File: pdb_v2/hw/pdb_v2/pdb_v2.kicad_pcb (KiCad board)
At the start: 4 copper layers, 96 x 56 mm, 75 parts, among them J1 XT30-M_Ver, J2 JST-PH_01x02, J3 Conn_01x06_Pin, J4 JST-PH_01x02, J5 JST-PH_01x02, J6 Conn_01x03, J7 Conn_01x03, J8 Conn_01x04, Q1 60Vds, SW1 SW_Push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

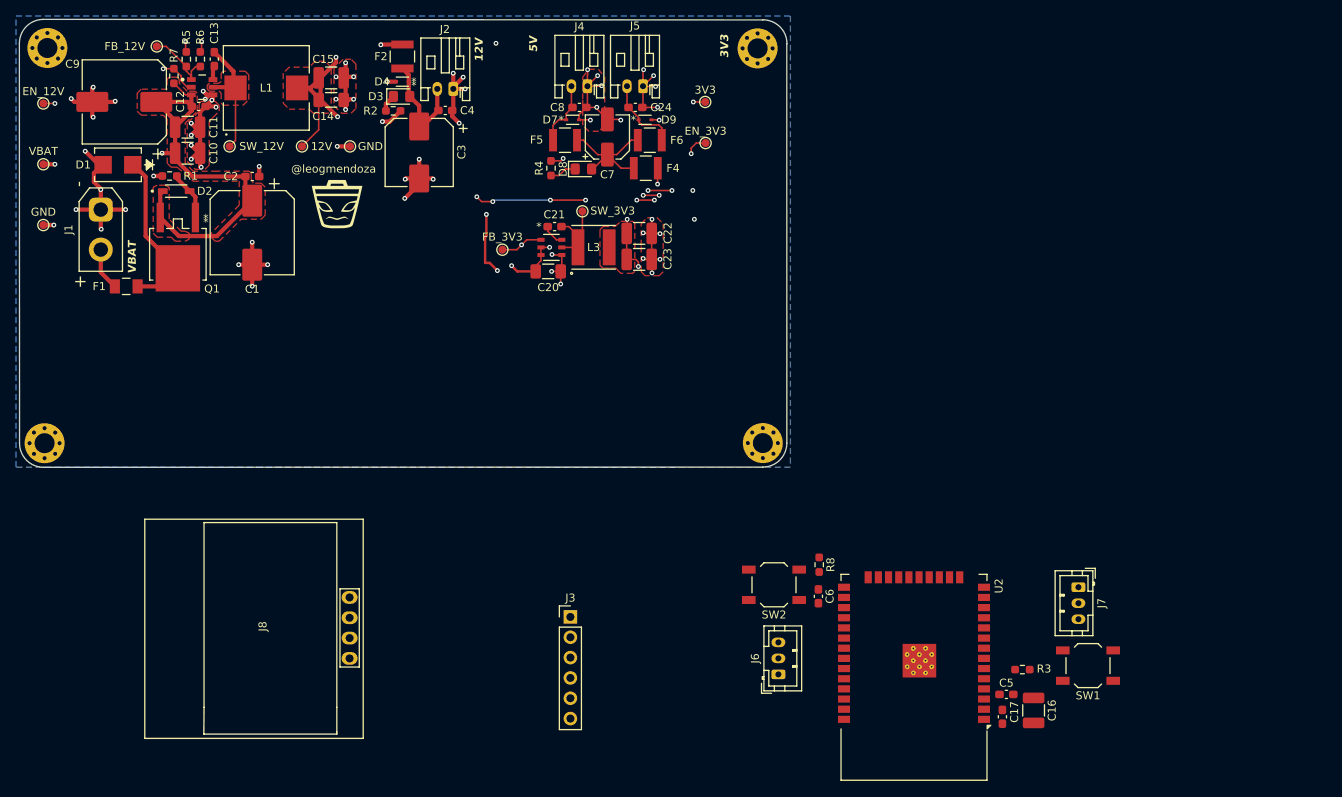
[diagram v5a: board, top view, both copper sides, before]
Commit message: removed second 3v3 connector, arranged telemetry components
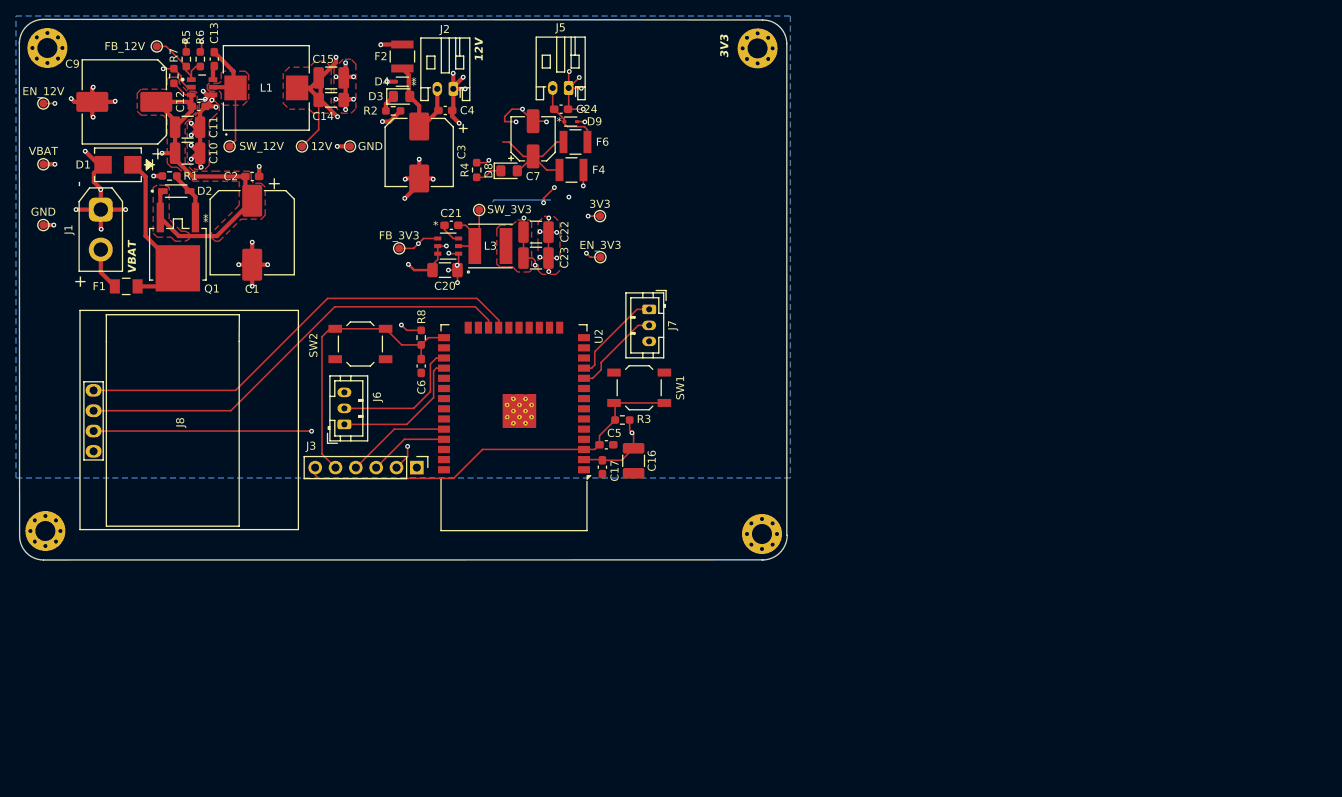
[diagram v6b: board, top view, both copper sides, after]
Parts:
- removed C8: 0.1uF, Capacitor_SMD:C_0603_1608Metric_Pad1.08x0.95mm_HandSolder
- removed D7: 3.3Vrwm, ESD5Z5.0T1G:SOD-523_0P9X1P3_ONS
- removed F5: 0.5A 16V, 0ZCH0050FF2G:0ZCH_BEL
- removed the G*** at (51.7, 35.1)
- removed J4: JST-PH_01x02, Connector_JST:JST_PH_S2B-PH-K_1x02_P2.00mm_Horizontal
- moved SW1 66.0 mm to (89.5, 58.1), turned to 0 degrees
- moved J7 63.9 mm to (90.8, 48.3)
- moved J6 62.6 mm to (52.6, 62.6)
- moved SW2 59.8 mm to (54.6, 52.6)
- moved C16 58.9 mm to (88.8, 67.2)
- moved C17 58.9 mm to (84.9, 68.0)
- moved C5 58.9 mm to (85.4, 65.2)
- moved R3 58.9 mm to (87.4, 62.1)
- moved U2 58.9 mm to (73.8, 60.1)
- moved C6 57.4 mm to (62.2, 55.4)
- moved R8 57.3 mm to (62.2, 51.8)
- moved J8 27.7 mm to (31.9, 62.4), turned to 90 degrees
- moved J3 26.8 mm to (61.7, 68.0), turned to -90 degrees
- moved 3V3 19.4 mm to (84.6, 36.6)
- moved EN_3V3 19.4 mm to (84.7, 41.8)
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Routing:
- net 3V3_BUS: track 57.1 -> 165.1 mm, vias 5 -> 11
- net 12V_BUS: track 205.2 -> 117.4 mm, vias 22 -> 8
- net /OLED SDA: track 0.00 -> 57.5 mm
- net /OLED SCL: track 0.00 -> 56.4 mm
- net /EN: track 0.00 -> 50.8 mm
- net /BOOT: track 0.00 -> 35.7 mm
- net /BMS TX: track 0.00 -> 17.3 mm
- net /BMS RX: track 0.00 -> 17.1 mm
- net /RX: track 0.00 -> 13.0 mm
- net /VESC TX: track 0.00 -> 12.2 mm
- net /VESC RX: track 0.00 -> 11.4 mm
- net /TX: track 0.00 -> 9.95 mm
- net Net-(J4-Pin_2): track 8.36 -> 0.00 mm
- net GND: track 144.3 -> 138.9 mm, vias 64 -> 62
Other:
- board size 96 x 56 mm -> 96 x 67.6 mm
- board text removed: "*"
- board text removed: "5V"
- board text removed: "@leogmendoza"

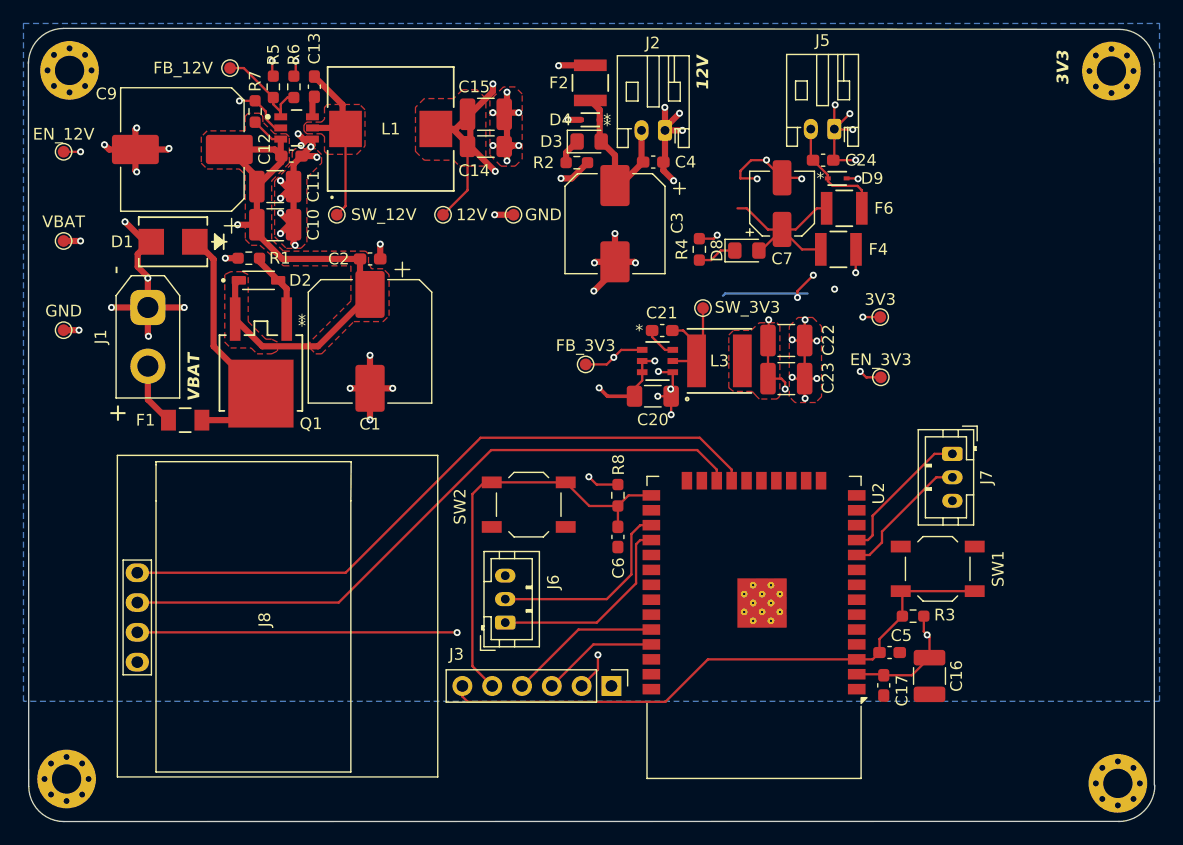
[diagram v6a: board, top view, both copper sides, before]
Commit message: fixed drc errors
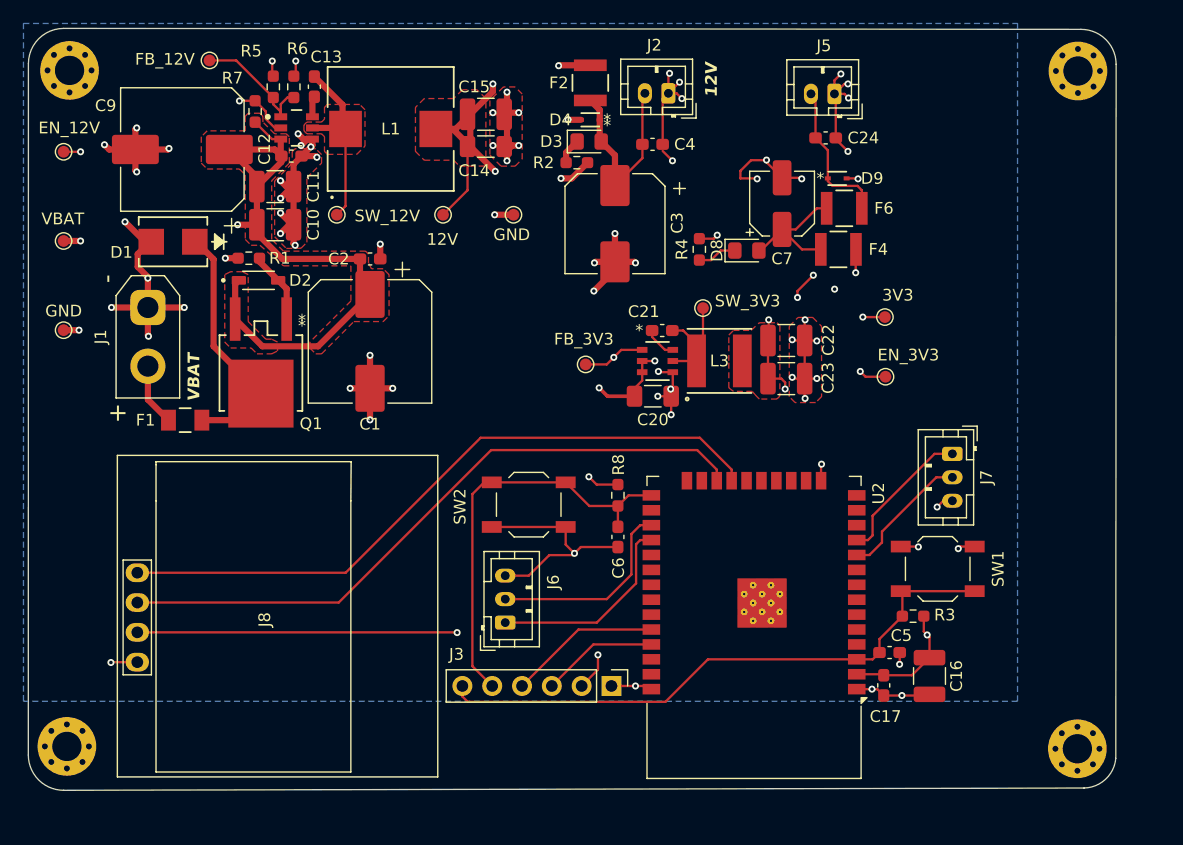
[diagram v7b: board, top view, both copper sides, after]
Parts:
- J2, J5: footprint Connector_JST:JST_PH_S2B-PH-K_1x02_P2.00mm_Horizontal -> Connector_JST:JST_PH_B2B-PH-K_1x02_P2.00mm_Vertical
- moved H4 4.54 mm to (101.4, 73.4)
- moved J2 3.17 mm to (66.5, 17.6)
- moved J5 3.00 mm to (80.7, 17.6)
- moved H2 2.85 mm to (101.5, 15.7)
- moved H3 2.78 mm to (15.3, 73.2)
- moved C24 1.91 mm to (80.0, 21.4)
- moved FB_12V1 1.87 mm to (27.4, 14.8)
- moved C4 1.51 mm to (65.2, 21.9)
- moved EN_3V3 0.40 mm to (85.0, 41.7)
- moved 3V3 0.40 mm to (85.0, 36.6)
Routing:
- net GND: track 138.9 -> 174.5 mm, vias 62 -> 72
- net 3V3_BUS: track 165.1 -> 158.2 mm
- net /3V3_SPLIT: track 15.8 -> 11.3 mm
- net Net-(D3-A): track 14.2 -> 17.5 mm
- net Net-(J5-Pin_2): track 9.79 -> 12.8 mm
- net Net-(U1-FB): track 9.05 -> 11.1 mm
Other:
- board size 96 x 67.6 mm -> 92.7 x 64.9 mm
- board text removed: "3V3"

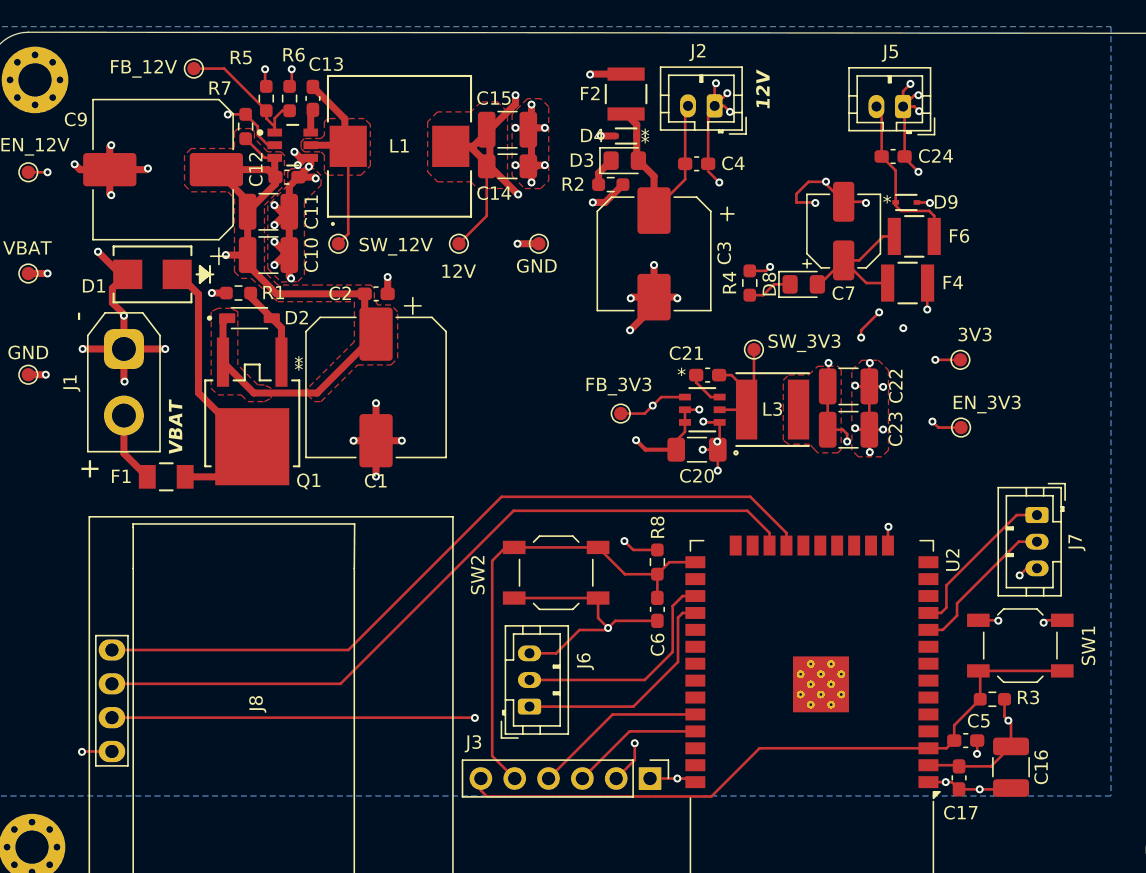
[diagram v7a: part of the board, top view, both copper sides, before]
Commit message: changed the dimensions of L1
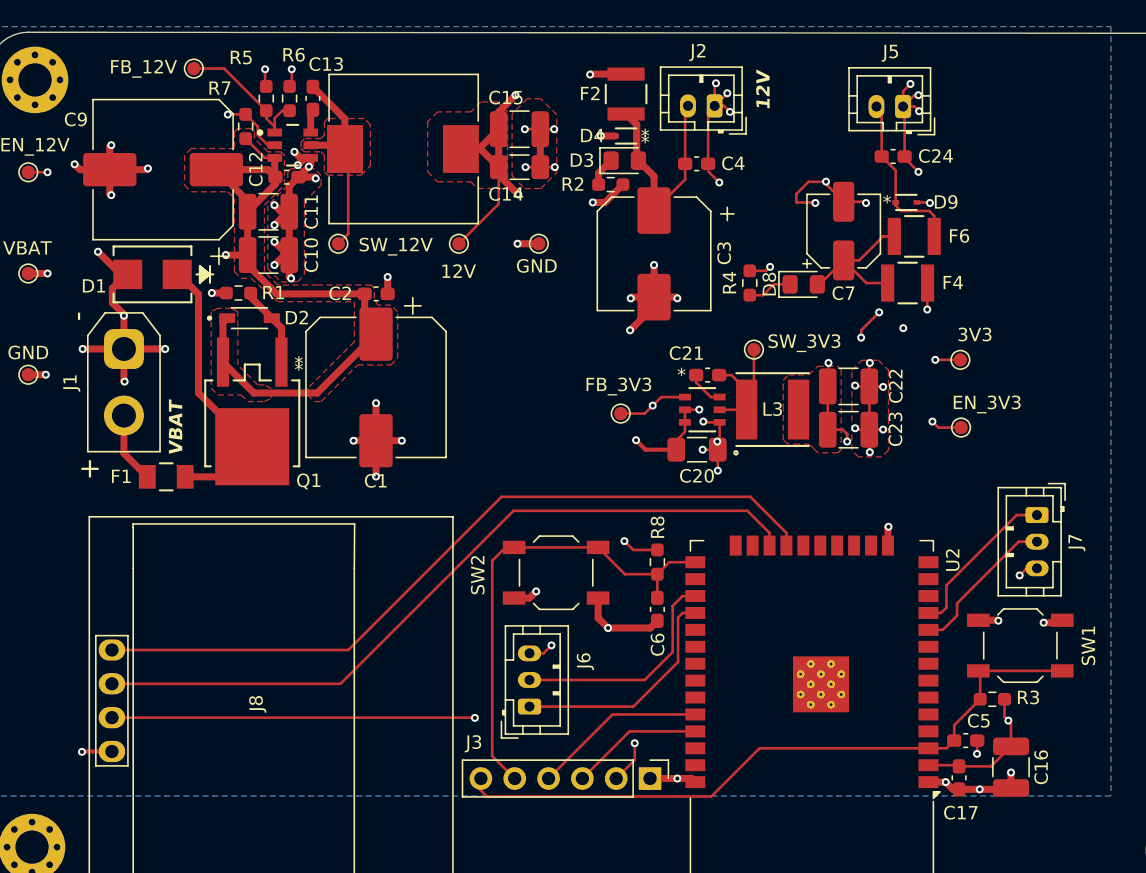
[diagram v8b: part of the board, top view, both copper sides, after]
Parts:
- moved C14 0.90 mm to (51.9, 22.1)
- moved C15 0.90 mm to (51.9, 19.3)
- moved L1 0.11 mm to (43.0, 20.6)
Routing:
- net GND: track 174.5 -> 165.4 mm, vias 72 -> 73
- net 12V_BUS: track 117.5 -> 120.3 mm
